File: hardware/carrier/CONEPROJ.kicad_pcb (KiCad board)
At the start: 4 copper layers, 86.1 x 99.5 mm, 85 parts, among them J2 Conn_02x15_Odd_Even_Shielded, J3 Conn_02x15_Odd_Even_Shielded, J304 U.FL-R-SMT-1(10), J4 DTM1312PA12PBR008, J5 TC2030-IDC, J6 UC-31PFFP-QS8001, J7 Conn_02x15_Odd_Even_Shielded, J8 Conn_02x15_Odd_Even_Shielded, Q2 Q_Dual_NMOS_S1G1S2G2D2D2D1D1, Q3 Q_Dual_NMOS_S1G1S2G2D2D2D1D1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

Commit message: backup
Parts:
- removed J3, J7, J8: Conn_02x15_Odd_Even_Shielded, TE_DTM1312PA12PBR008:PinSocket_2x16_P1.27mm_Vertical_SMD
- removed J6: UC-31PFFP-QS8001, AMPHENOL_UC-31PFFP-QS8001:AMPHENOL_UC-31PFFP-QS8001
- removed R2, R8: 5.1k, Resistor_SMD:R_0603_1608Metric_Pad0.98x0.95mm_HandSolder
- added JP10: Jumper_2_Open, Jumper:SolderJumper-2_P1.3mm_Open_RoundedPad1.0x1.5mm, B.Cu at (40.2, 69.2)
- added JP11: Jumper_2_Open, Jumper:SolderJumper-2_P1.3mm_Open_RoundedPad1.0x1.5mm, B.Cu at (42.2, 89.1)
- added JP2: Jumper_2_Open, Jumper:SolderJumper-2_P1.3mm_Open_RoundedPad1.0x1.5mm, F.Cu at (71.3, 66.2)
- added JP3: Jumper_2_Open, Jumper:SolderJumper-2_P1.3mm_Open_RoundedPad1.0x1.5mm, F.Cu at (71.3, 67.9)
- added JP6: Jumper_2_Open, Jumper:SolderJumper-2_P1.3mm_Open_RoundedPad1.0x1.5mm, B.Cu at (48.2, 69.1)
- added JP7: Jumper_2_Open, Jumper:SolderJumper-2_P1.3mm_Open_RoundedPad1.0x1.5mm, B.Cu at (46.2, 69.1)
- added JP8: Jumper_2_Open, Jumper:SolderJumper-2_P1.3mm_Open_RoundedPad1.0x1.5mm, B.Cu at (44.2, 69.1)
- added JP9: Jumper_2_Open, Jumper:SolderJumper-2_P1.3mm_Open_RoundedPad1.0x1.5mm, B.Cu at (42.2, 69.2)
- C302, D301, D302, R11, R12, R21, R22: moved to F.Cu
- moved R12 38.6 mm to (69.7, 67.6)
- moved R11 35.9 mm to (69.7, 66.5)
- moved R21 35.0 mm to (72.1, 79.6), turned to 0 degrees
- moved R22 34.5 mm to (75.1, 73.0), turned to 90 degrees
- moved D308 27.5 mm to (76.7, 76.6), turned to -90 degrees
- moved R91 27.4 mm to (76.7, 73.0), turned to 90 degrees
- moved D302 26.4 mm to (72.9, 77.0), turned to 0 degrees
- moved D301 24.4 mm to (75.1, 76.5), turned to 90 degrees
- moved C302 8.84 mm to (46.9, 70.2)
- moved J304 8.17 mm to (31.4, 78.7)
- moved U310 3.39 mm to (45.2, 79.1)
- moved PAU301 1.46 mm to (57.3, 71.5)
- moved MOD301 1.16 mm to (57.3, 77.0)
- moved J2 0.25 mm to (43.0, 84.5)
- turned C21 to 90 degrees
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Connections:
- C3 pad 1: /VIN -> /EXT_12V
- D2 pad 1: /VIN -> /EXT_12V
- J2 pad 1: unconnected-(J2-Pad1) -> GND
- J2 pad 10: unconnected-(J2-Pad10) -> /EXT_IO1
- J2 pad 11: unconnected-(J2-Pad11) -> /TXD3
- J2 pad 12: unconnected-(J2-Pad12) -> /EXT_IO2
- J2 pad 13: unconnected-(J2-Pad13) -> /EXT_UART_RTS
- J2 pad 14: unconnected-(J2-Pad14) -> /EXT_IO3
- J2 pad 15: unconnected-(J2-Pad15) -> /EXT_UART_CTS
- J2 pad 16: unconnected-(J2-Pad16) -> /EXT_IO4
- J2 pad 18: unconnected-(J2-Pad18) -> /EXT_IO5
- J2 pad 2: unconnected-(J2-Pad2) -> /EXT_12V
- J2 pad 20: unconnected-(J2-Pad20) -> /EXT_SPI_MISO
- J2 pad 22: unconnected-(J2-Pad22) -> /EXT_SPI_MOSI
- J2 pad 24: unconnected-(J2-Pad24) -> /EXT_SPI_SCK
- J2 pad 26: unconnected-(J2-Pad26) -> /EXT_SPI_SS0
- J2 pad 27: unconnected-(J2-Pad27) -> /EXT_I2C_SCL
- J2 pad 28: unconnected-(J2-Pad28) -> /EXT_SPI_SS1
- J2 pad 29: unconnected-(J2-Pad29) -> /EXT_I2C_SDA
- J2 pad 3: unconnected-(J2-Pad3) -> +3V3
- J2 pad 30: unconnected-(J2-Pad30) -> /EXT_SPI_SS2
- J2 pad 4: unconnected-(J2-Pad4) -> +5V
- J2 pad 6: unconnected-(J2-Pad6) -> /EXT_CAN_TX
- J2 pad 8: unconnected-(J2-Pad8) -> /EXT_CAN_RX
- J2 pad 9: unconnected-(J2-Pad9) -> /RXD3
- J4 pad B6: /VIN -> /EXT_12V
- R11 pad 1: /I2C1_SDA -> /EXT_I2C_SDA
- R12 pad 1: /I2C1_SCL -> /EXT_I2C_SCL
- U10 pad 11: /GPO_4 -> unconnected-(U10-Pad11)
- U10 pad 12: /GPO_5 -> unconnected-(U10-Pad12)
- U10 pad 13: /GPO_6 -> unconnected-(U10-Pad13)
- U10 pad 14: /GPO_3 -> unconnected-(U10-Pad14)
- U10 pad 15: /GPO_2 -> unconnected-(U10-Pad15)
- U10 pad 16: /GPO_1 -> unconnected-(U10-Pad16)
- U10 pad 17: /LEDA -> unconnected-(U10-Pad17)
- U10 pad 2: /GPO_7 -> /RP2040_SPI_RX
- U10 pad 3: /GPO_8 -> /RP2040_SPI_CSn
- U10 pad 4: /GPO_9 -> /RP2040_SPI_SCK
- U10 pad 5: /LEDR -> /RP2040_SPI_TX
- U10 pad 6: /I2C1_SDA -> unconnected-(U10-Pad6)
- U10 pad 7: /I2C1_SCL -> /RP2040_I2C_SDA
- U10 pad 8: /LEDG -> /RP2040_I2C_SCL
- U10 pad 9: /LEDB -> unconnected-(U10-Pad9)
- U304 pad 1: /VIN -> /EXT_12V
- U310 pad 14: /RF69_INT -> /EXT_IO1
- U310 pad 2: /RF69_MISO -> /EXT_SPI_MISO
- U310 pad 3: /RF69_MOSI -> /EXT_SPI_MOSI
- U310 pad 4: /RF69_SCK -> /EXT_SPI_SCK
- U310 pad 5: /RF69_NSS -> /EXT_SPI_SS0
- U310 pad 6: /RF69_RESET -> /EXT_IO2
- U5 pad 13: /MCP_INT -> /EXT_IO3
- U5 pad 14: /SPI0_SCLK -> /EXT_SPI_SCK
- U5 pad 16: /SPI0_MOSI -> /EXT_SPI_MOSI
- U5 pad 17: /SPI0_MISO -> /EXT_SPI_MISO
- U5 pad 18: /SPI0_CE0_N -> /EXT_SPI_SS1
- U8 pad 12: /MCP_INT -> /EXT_IO3
- U8 pad 13: /SPI0_SCLK -> /EXT_SPI_SCK
- U8 pad 14: /SPI0_MOSI -> /EXT_SPI_MOSI
- U8 pad 15: /SPI0_MISO -> /EXT_SPI_MISO
- U8 pad 16: /SPI0_CE0_N -> /EXT_SPI_SS1
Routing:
- net unconnected-(R23-Pad1): track 0.00 -> 65.8 mm, vias 0 -> 1
- net /GPO_5: track 65.8 -> 0.00 mm, vias 1 -> 0
- net unconnected-(R31-Pad1): track 0.00 -> 48.5 mm, vias 0 -> 1
- net /GPO_2: track 48.5 -> 0.00 mm, vias 1 -> 0
- net unconnected-(R303-Pad1): track 0.00 -> 43.1 mm, vias 0 -> 1
- net /GPO_1: track 43.1 -> 0.00 mm, vias 1 -> 0
- net unconnected-(R14-Pad1): track 0.00 -> 28.6 mm, vias 0 -> 1
- net /GPO_7: track 28.6 -> 0.00 mm, vias 1 -> 0
- net unconnected-(U10-Pad6): track 0.00 -> 27.3 mm, vias 0 -> 2
- net /I2C1_SDA: track 64.9 -> 37.6 mm, vias 3 -> 1
- net unconnected-(R10-Pad1): track 0.00 -> 26.7 mm, vias 0 -> 1
- net /GPO_8: track 26.7 -> 0.00 mm, vias 1 -> 0
- net /I2C1_SCL: track 59.9 -> 33.9 mm, vias 3 -> 1
- net /RP2040_I2C_SDA: track 0.00 -> 26.0 mm, vias 0 -> 2
- net unconnected-(R13-Pad1): track 0.00 -> 23.3 mm, vias 0 -> 1
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- added copper zone on F.Cu, net /EXT_12V
- removed copper zone on F.Cu, net /VIN

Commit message: asdf
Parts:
- removed JP10, JP11, JP2, JP3, JP6, JP7, JP8, JP9: Jumper_2_Open, Jumper:SolderJumper-2_P1.3mm_Open_RoundedPad1.0x1.5mm
- removed R10, R13, R14, R23, R24, R27, R29, R302, R303, R304, R31, R9: 100k, Resistor_SMD:R_0603_1608Metric_Pad0.98x0.95mm_HandSolder
- C302, J304, R11, R12: moved to B.Cu
- moved J2 23.9 mm to (67.0, 84.3)
- moved C302 20.8 mm to (30.2, 82.5), turned to 90 degrees
- moved MOD301 16.4 mm to (43.0, 85.1)
- moved PAU301 16.4 mm to (43.0, 79.6)
- moved R21 10.1 mm to (81.3, 75.6)
- moved J304 9.84 mm to (30.2, 88.5)
- moved R22 8.59 mm to (81.3, 78.9), turned to 0 degrees
- moved R91 6.25 mm to (81.3, 77.3), turned to 0 degrees
- moved R11 5.80 mm to (74.5, 63.2), turned to -90 degrees
- moved R12 5.72 mm to (73.4, 63.2), turned to -90 degrees
- moved D302 5.01 mm to (77.7, 75.6), turned to 180 degrees
- moved U310 4.01 mm to (43.0, 82.5), turned to 180 degrees
- moved D301 3.59 mm to (77.8, 78.9), turned to 180 degrees
- moved D308 1.26 mm to (77.7, 77.3), turned to 180 degrees
- moved C21 0.53 mm to (59.1, 52.1)
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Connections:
- J2 pad 1: GND -> +5V
- J2 pad 10: /EXT_IO1 -> /EXT_I2C_SDA
- J2 pad 11: /TXD3 -> /CAN_RX
- J2 pad 12: /EXT_IO2 -> /EXT_I2C_SCL
- J2 pad 13: /EXT_UART_RTS -> +3V3
- J2 pad 14: /EXT_IO3 -> GND
- J2 pad 15: /EXT_UART_CTS -> +3V3
- J2 pad 16: /EXT_IO4 -> GND
- J2 pad 17: unconnected-(J2-Pad17) -> +3V3
- J2 pad 18: /EXT_IO5 -> GND
- J2 pad 19: unconnected-(J2-Pad19) -> /MODE_BTN
- J2 pad 2: /EXT_12V -> +3V3
- J2 pad 20: /EXT_SPI_MISO -> /EXT_IO3
- J2 pad 21: unconnected-(J2-Pad21) -> /PAUSE_BTN
- J2 pad 22: /EXT_SPI_MOSI -> /EXT_SPI_SS1
- J2 pad 24: /EXT_SPI_SCK -> /EXT_SPI_MISO
- J2 pad 26: /EXT_SPI_SS0 -> /EXT_SPI_MOSI
- J2 pad 27: /EXT_I2C_SCL -> /EXT_12V
- J2 pad 28: /EXT_SPI_SS1 -> /EXT_SPI_SCK
- J2 pad 29: /EXT_I2C_SDA -> /EXT_12V
- J2 pad 3: +3V3 -> +5V
- J2 pad 30: /EXT_SPI_SS2 -> /EXT_SPI_SS0
- J2 pad 31: (no net) -> /EXT_IO1
- J2 pad 32: (no net) -> /EXT_IO2
- J2 pad 4: +5V -> /LED_GRN
- J2 pad 5: unconnected-(J2-Pad5) -> /EXT_UART_RX
- J2 pad 6: /EXT_CAN_TX -> /WIFI_LED
- J2 pad 7: unconnected-(J2-Pad7) -> /EXT_UART_TX
- J2 pad 8: /EXT_CAN_RX -> /LED_RED
- J2 pad 9: /RXD3 -> /CAN_TX
- J4 pad B10: /I2C1_SCL -> /EXT_I2C_SCL
- J4 pad B11: /TXD3 -> /EXT_UART_TX
- J4 pad B12: /RXD3 -> /EXT_UART_RX
- J4 pad B9: /I2C1_SDA -> /EXT_I2C_SDA
- U10 pad 11: unconnected-(U10-Pad11) -> /GPO_4
- U10 pad 27: unconnected-(U10-Pad27) -> /EXT_SPI_MISO
- U10 pad 28: unconnected-(U10-Pad28) -> /EXT_SPI_SS1
- U10 pad 29: unconnected-(U10-Pad29) -> /EXT_SPI_SCK
- U10 pad 3: /RP2040_SPI_CSn -> /GPO_8
- U10 pad 30: unconnected-(U10-Pad30) -> /EXT_SPI_MOSI
- U10 pad 4: /RP2040_SPI_SCK -> /GPO_9
- U10 pad 5: /RP2040_SPI_TX -> /LEDR
- U10 pad 6: unconnected-(U10-Pad6) -> /EXT_I2C_SCL
- U10 pad 7: /RP2040_I2C_SDA -> /EXT_I2C_SDA
- U10 pad 8: /RP2040_I2C_SCL -> /LEDG
- U10 pad 9: unconnected-(U10-Pad9) -> /LEDB
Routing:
- net /EXT_I2C_SDA: track 0.00 -> 112.4 mm, vias 0 -> 4
- net /EXT_I2C_SCL: track 0.00 -> 108.9 mm, vias 0 -> 4
- net /EXT_UART_RX: track 0.00 -> 85.1 mm, vias 0 -> 2
- net /EXT_UART_TX: track 0.00 -> 83.4 mm, vias 0 -> 2
- net unconnected-(R23-Pad1): track 65.8 -> 0.00 mm, vias 1 -> 0
- net /CAN_RX: track 30.3 -> 94.7 mm, vias 0 -> 2
- net /GPO_6: track 59.8 -> 0.00 mm, vias 1 -> 0
- net +5V: track 0.00 -> 59.5 mm, vias 4 -> 7
- net /GPO_3: track 56.5 -> 0.00 mm, vias 1 -> 0
- net /CAN_TX: track 37.2 -> 92.4 mm, vias 0 -> 2
- net /EXT_SPI_MISO: track 0.04 -> 51.8 mm, vias 0 -> 3
- net /EXT_12V: track 6.04 -> 55.0 mm, vias 0 -> 8
- net /EXT_SPI_MOSI: track 0.11 -> 49.0 mm, vias 0 -> 3
- net unconnected-(R31-Pad1): track 48.5 -> 0.00 mm, vias 1 -> 0
- net /EXT_SPI_SCK: track 0.04 -> 47.6 mm, vias 0 -> 3
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- added copper zone on B.Cu, net +3V3
- added copper zone on B.Cu, net GND
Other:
- board size 86.1 x 99.5 mm -> 86 x 50 mm

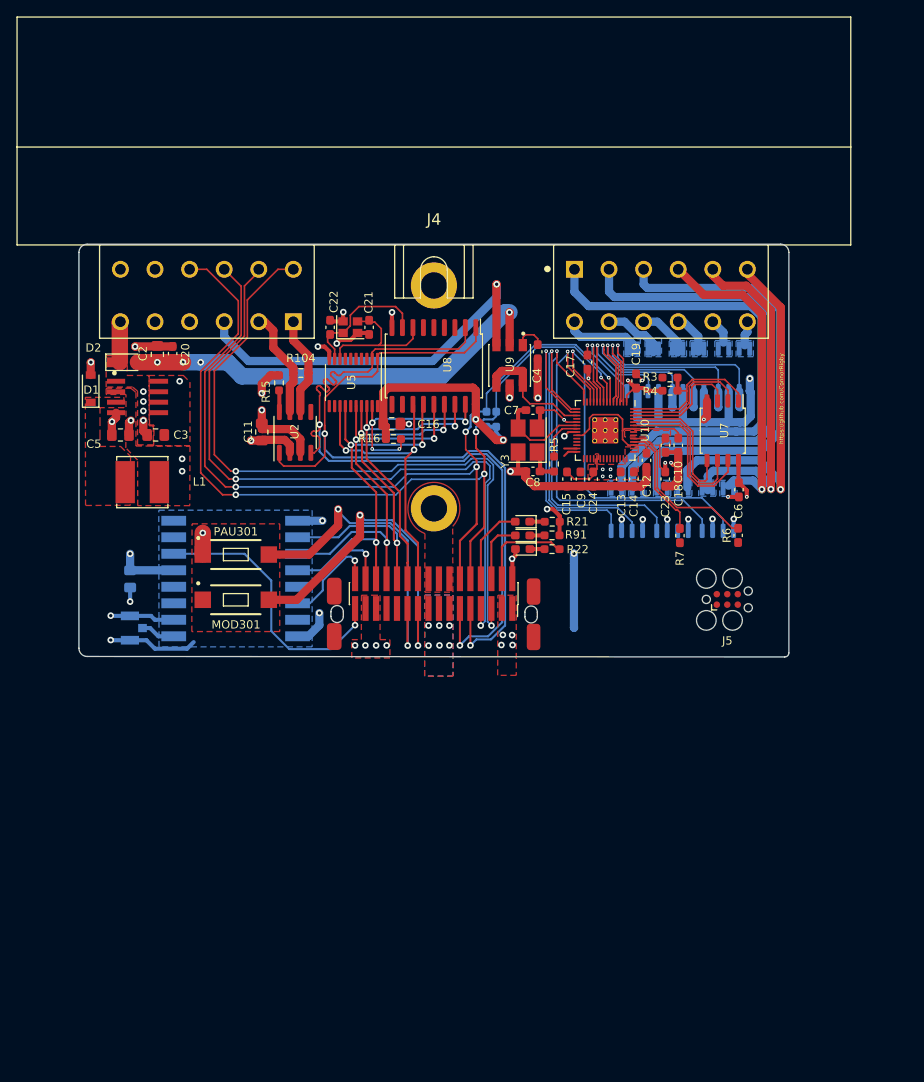
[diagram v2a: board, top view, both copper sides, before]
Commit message: almost Finish carrier board
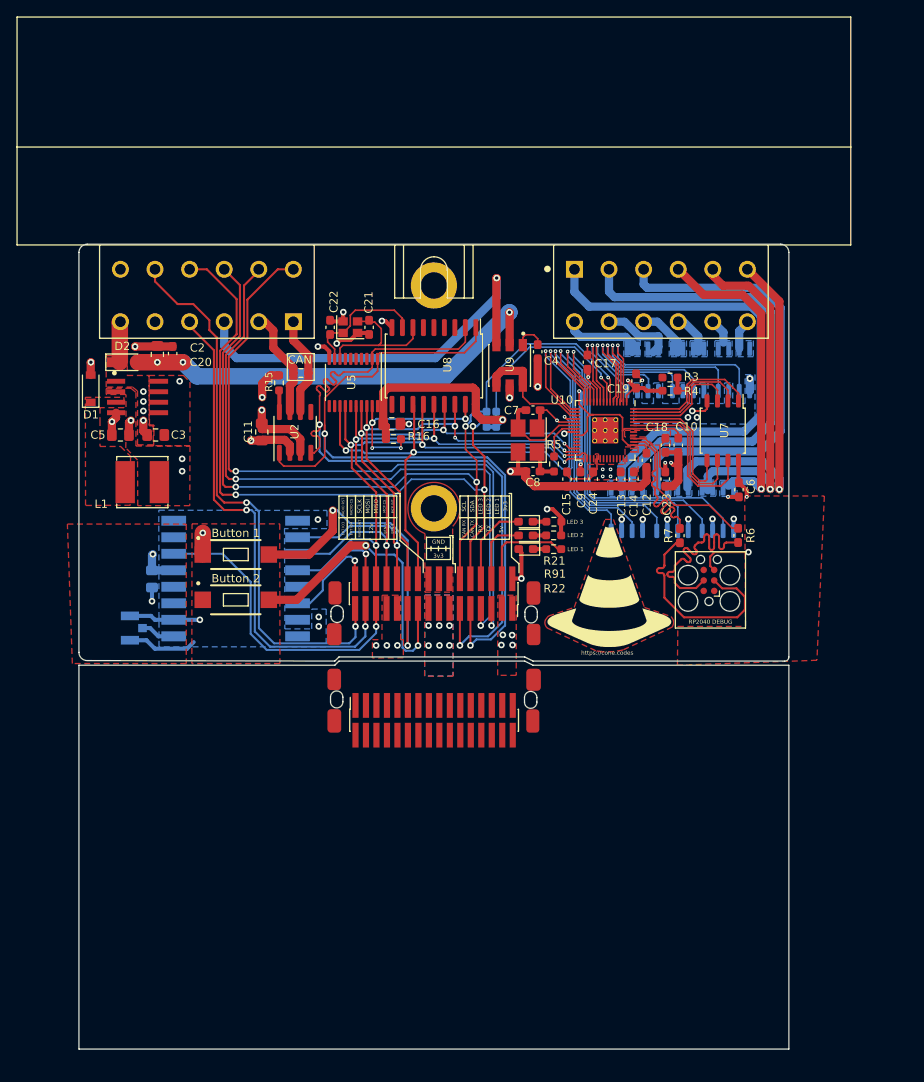
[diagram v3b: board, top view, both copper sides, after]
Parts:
- added G***: LOGO, logos:cone, F.Cu at (88.2, 83.5)
- added J2: Conn_02x15_Odd_Even_Shielded, TE_DTM1312PA12PBR008:PinSocket_2x16_P1.27mm_Vertical_SMD, F.Cu at (67.0, 99.7)
- moved J5 3.20 mm to (100.3, 82.7), turned to 90 degrees
- moved C302 2.65 mm to (32.9, 82.5)
- moved D301 0.40 mm to (78.2, 78.9)
- moved D302 0.40 mm to (78.1, 75.6)
- moved D308 0.40 mm to (78.1, 77.3)
- moved R21 0.20 mm to (81.5, 75.6)
- moved R22 0.20 mm to (81.5, 78.9)
- moved R91 0.20 mm to (81.5, 77.3)
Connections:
- net /PICO_USB_DP renamed /PICO_USB_P
- net Net-(R6-Pad1) renamed /PICO_USB__P
- net Net-(R7-Pad2) renamed /PICO_USB__N
- J2 pad 23: unconnected-(J2-Pad23) -> /EXT_12V
- J2 pad 25: unconnected-(J2-Pad25) -> /EXT_12V
- J2 pad 27: /EXT_12V -> /EXT_IO1
- J2 pad 29: /EXT_12V -> /EXT_IO4
- J2 pad 31: /EXT_IO1 -> /EXT_IO5
- J2 pad MP: unconnected-(J2-PadMP) -> (no net)
- J4 pad B4: unconnected-(J4-PadB4) -> /EXT_IO4
- J4 pad B5: unconnected-(J4-PadB5) -> +5V
- J4 pad B8: unconnected-(J4-PadB8) -> /EXT_IO5
- J5 pad 2: /PICO_USB_DM -> unconnected-(J5-Pad2)
- J5 pad 3: unconnected-(J5-Pad3) -> /PICO_USB_N
- R7 pad 1: /PICO_USB_DM -> /PICO_USB_N
- U10 pad 12: unconnected-(U10-Pad12) -> /GPO_12
- U10 pad 13: unconnected-(U10-Pad13) -> /GPO_6
- U10 pad 14: unconnected-(U10-Pad14) -> /GPO_3
- U10 pad 15: unconnected-(U10-Pad15) -> /GPO_2
- U10 pad 16: unconnected-(U10-Pad16) -> /GPO_1
- U10 pad 17: unconnected-(U10-Pad17) -> /LEDA
- U10 pad 18: unconnected-(U10-Pad18) -> /EXT_IO3
- U10 pad 2: /RP2040_SPI_RX -> /GPO_7
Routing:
- net /EXT_IO5: track 0.00 -> 67.9 mm, vias 0 -> 2
- net /EXT_IO4: track 0.00 -> 60.8 mm, vias 0 -> 2
- net unconnected-(U10-Pad12): track 45.6 -> 0.00 mm, vias 1 -> 0
- net /GPO_12: track 0.00 -> 42.1 mm, vias 0 -> 1
- net unconnected-(U10-Pad14): track 41.5 -> 0.00 mm, vias 1 -> 0
- net /GPO_6: track 0.00 -> 41.0 mm, vias 0 -> 1
- net GND: track 162.7 -> 123.5 mm, vias 34 -> 37
- net /GPO_3: track 0.00 -> 38.8 mm, vias 0 -> 1
- net unconnected-(U10-Pad16): track 38.1 -> 0.00 mm, vias 1 -> 0
- net /GPO_1: track 0.00 -> 35.9 mm, vias 0 -> 1
- net /RP2040_SPI_RX: track 28.6 -> 0.00 mm, vias 1 -> 0
- net /EXT_IO3: track 36.5 -> 64.0 mm, vias 2 -> 3
- net /GPO_7: track 0.00 -> 26.6 mm, vias 0 -> 1
- net /PICO_USB_N: track 0.00 -> 26.2 mm
- net /PICO_USB_P: track 0.00 -> 25.9 mm
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- added copper zone on F.Cu, net (none)
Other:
- board size 86 x 50 mm -> 86 x 97.5 mm
- board text added: "12V"
- board text added: "12v"
- board text added: "3v3"
- board text added: "5V"
- board text added: "5v"
- board text added: "BTN 1"
- board text added: "BTN 2"
- board text added: "Button 1"
- board text added: "Button 2"
- board text added: "CAN"
- board text added: "CAN RGB CONTROLLER V3 Designed by Connor Rigby 2022"
- board text added: "CAN RX"
- board text added: "CAN TX"
- board text added: "CANH"
- board text added: "CANL"
- board text added: "EXT IO3"
- board text added: "EXT IO4"
- board text added: "GND"
- board text added: "GPO1"
- board text added: "GPO2"
- board text added: "GPO3"
- board text added: "GPO4"
- board text added: "GPO5"
- board text added: "GPO6"
- board text added: "GPO7"
- board text added: "GPO8"
- board text added: "GPO9"
- board text added: "GPOB"
- board text added: "GPOG"
- board text added: "GPOR"
- board text added: "IO4"
- board text added: "IO5"
- board text added: "LED 1"
- board text added: "LED 2"
- board text added: "LED 3"
- board text added: "LEDA"
- board text added: "LOW SIDE DRIVERS"
- board text added: "MCP CS"
- board text added: "MCP INT"
- board text added: "MISO"
- board text added: "MOSI"
- board text added: "POWER I/O"
- board text added: "RADIO CS"
- board text added: "RADIO INT"
- board text added: "RADIO RST"
- board text added: "RP2040 DEBUG"
- board text added: "RX"
- board text added: "SCL"
- board text added: "SCLK"
- board text added: "SDA"
- board text added: "TX"
- board text added: "https://cone.codes"

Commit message: Carrier submitted to assembly
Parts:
- removed the J2 at (67.0, 99.7)
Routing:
- net /GPO_8_OUT: track 3.07 -> 4.14 mm
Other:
- board size 86 x 97.5 mm -> 86 x 50.5 mm
- board text added: "JLCJLCJLCJLC"
